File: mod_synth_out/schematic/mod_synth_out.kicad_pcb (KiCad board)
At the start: 2 copper layers, 74.3 x 109.2 mm, 64 parts, among them J1 L IN, J2 R IN, J3 Conn_02x08_Odd_Even, J4 Phones, J5 L OUT, J6 R OUT, Q1 2N3904, Q2 2N3904, U1 TL072, U2 TL072, U3 NE5532, U4 NE5532

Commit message: Attmept layout of output pcb on large pcb
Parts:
- added J7: Conn_01x07_Female, Connector_PinSocket_2.54mm:PinSocket_1x07_P2.54mm_Vertical, F.Cu at (207.6, 79.4)
- added J8: Conn_01x07_Male, Connector_PinHeader_2.54mm:PinHeader_1x07_P2.54mm_Vertical, B.Cu at (250.2, 79.4)
- C1, C10, C11, C12, C13, C14, C15, C16, C2, C3, C4, C5, C6, C7, C8, C9, D1, D2, D3, D4, D7, D8, FB1, FB2, J3, Q1, Q2, R1, R10, R11, R12, R13, R14, R15, R16, R17, R18, R19, R2, R20, R21, R22, R23, R24, R3, R4, R5, R6, R7, R8, R9, U1, U2, U3, U4: moved to B.Cu
- moved D1 218.8 mm to (233.0, 45.7), turned to 270 degrees
- moved R2 217.4 mm to (275.6, 83.2)
- moved D2 214.0 mm to (233.0, 35.6), turned to 270 degrees
- moved R18 194.0 mm to (217.8, 35.6), turned to 0 degrees
- moved J2 193.1 mm to (258.4, 61.6)
- moved RV2 191.8 mm to (265.4, 116.2)
- moved R1 190.1 mm to (248.9, 83.2)
- moved R17 185.2 mm to (210.2, 35.6), turned to 180 degrees
- moved D4 180.9 mm to (196.2, 35.6)
- moved D3 176.6 mm to (196.2, 53.3), turned to 90 degrees
- moved J1 175.4 mm to (242.6, 61.6)
- moved RV1 172.9 mm to (243.2, 116.2)
- moved J4 170.2 mm to (224.2, 132.7)
- moved J6 169.6 mm to (222.9, 45.7)
- moved R20 163.2 mm to (229.2, 55.9), turned to 180 degrees
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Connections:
- C10 pad 1: GND -> /GND_PCB_B
- C10 pad 2: +12V -> /+12_PCB_B
- C7 pad 1: -12V -> /-12_PCB_B
- C7 pad 2: GND -> /GND_PCB_B
- D5 pad 2: +12V -> /+12_PCB_B
- D6 pad 2: +12V -> /+12_PCB_B
- J1 pad S: GND -> /GND_PCB_B
- J2 pad S: GND -> /GND_PCB_B
- Q1 pad 1: GND -> /GND_PCB_B
- Q2 pad 1: GND -> /GND_PCB_B
- RV1 pad 1: GND -> /GND_PCB_B
- RV1 pad 4: GND -> /GND_PCB_B
- RV2 pad 1: GND -> /GND_PCB_B
- RV2 pad 4: GND -> /GND_PCB_B
- U1 pad 3: GND -> /GND_PCB_B
- U1 pad 4: -12V -> /-12_PCB_B
- U1 pad 5: GND -> /GND_PCB_B
- U1 pad 8: +12V -> /+12_PCB_B
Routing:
- net +12V: track 0.00 -> 187.8 mm
- net -12V: track 0.00 -> 142.3 mm
- net Net-(C16-Pad1): track 0.00 -> 55.9 mm
- net Net-(C6-Pad2): track 0.00 -> 54.6 mm
- net Net-(C15-Pad1): track 0.00 -> 52.8 mm
- net /A_POT_PH_R: track 0.00 -> 51.6 mm
- net /A_POT_MR: track 0.00 -> 48.7 mm
- net Net-(C9-Pad2): track 0.00 -> 48.5 mm
- net Net-(C5-Pad1): track 0.00 -> 46.1 mm
- net /A_POT_ML: track 0.00 -> 44.3 mm
- net Net-(C8-Pad2): track 0.00 -> 44.1 mm
- net Net-(C6-Pad1): track 0.00 -> 43.7 mm
- net /A_POT_PH_L: track 0.00 -> 41.8 mm
- net Net-(R7-Pad1): track 0.00 -> 41.5 mm
- net Net-(R10-Pad2): track 0.00 -> 41.2 mm
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- added copper zone on B.Cu, net /GND_PCB_B
- added copper zone on F.Cu, net /GND_PCB_B
- added copper zone on B.Cu, net GND
- added copper zone on F.Cu, net GND
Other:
- board size 74.3 x 109.2 mm -> 81.9 x 109.2 mm

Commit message: Finish huge output pcb
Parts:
- moved U3 10.8 mm to (201.3, 98.4), turned to 0 degrees
- moved U4 10.8 mm to (220.3, 98.4), turned to 0 degrees
- moved U1 10.3 mm to (253.4, 97.8), turned to 0 degrees
- moved D1 8.26 mm to (233.0, 54.0), turned to 90 degrees
- moved C8 2.54 mm to (248.3, 95.9), turned to 270 degrees
- moved C9 2.54 mm to (266.1, 95.9), turned to 270 degrees
- moved J7 0.64 mm to (207.0, 79.4)
- moved C7 0.64 mm to (254.6, 86.4)
- moved D2 0.63 mm to (233.0, 36.2)
- moved D3 0.63 mm to (196.2, 54.0)
- moved D4 0.63 mm to (196.2, 36.2)
- moved R17 0.63 mm to (210.2, 36.2)
- moved R18 0.63 mm to (217.8, 36.2)
- moved C5 0.63 mm to (241.9, 87.0)
- moved J8 0.63 mm to (249.6, 79.4)
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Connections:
- J5 pad S: Net-(J5-PadS) -> GND
- J6 pad S: Net-(J6-PadS) -> GND
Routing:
- net Net-(R14-Pad2): track 16.2 -> 48.2 mm
- net Net-(C6-Pad1): track 43.7 -> 15.1 mm
- net -12V: track 142.3 -> 170.7 mm
- net Net-(C6-Pad2): track 54.6 -> 26.7 mm
- net Net-(C5-Pad1): track 46.1 -> 22.5 mm
- net +12V: track 187.8 -> 164.3 mm
- net Net-(R7-Pad1): track 41.5 -> 20.7 mm
- net Net-(R10-Pad2): track 41.2 -> 20.7 mm
- net /GND_PCB_B: track 16.7 -> 0.00 mm
- net /+12_PCB_B: track 39.8 -> 52.5 mm
- net Net-(C5-Pad2): track 26.8 -> 15.6 mm
- net Net-(J4-PadT): track 38.7 -> 49.5 mm
- net Net-(R13-Pad2): track 7.93 -> 15.1 mm
- net Net-(R15-Pad2): track 7.93 -> 14.1 mm
- net /A_POT_ML: track 44.3 -> 39.5 mm
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
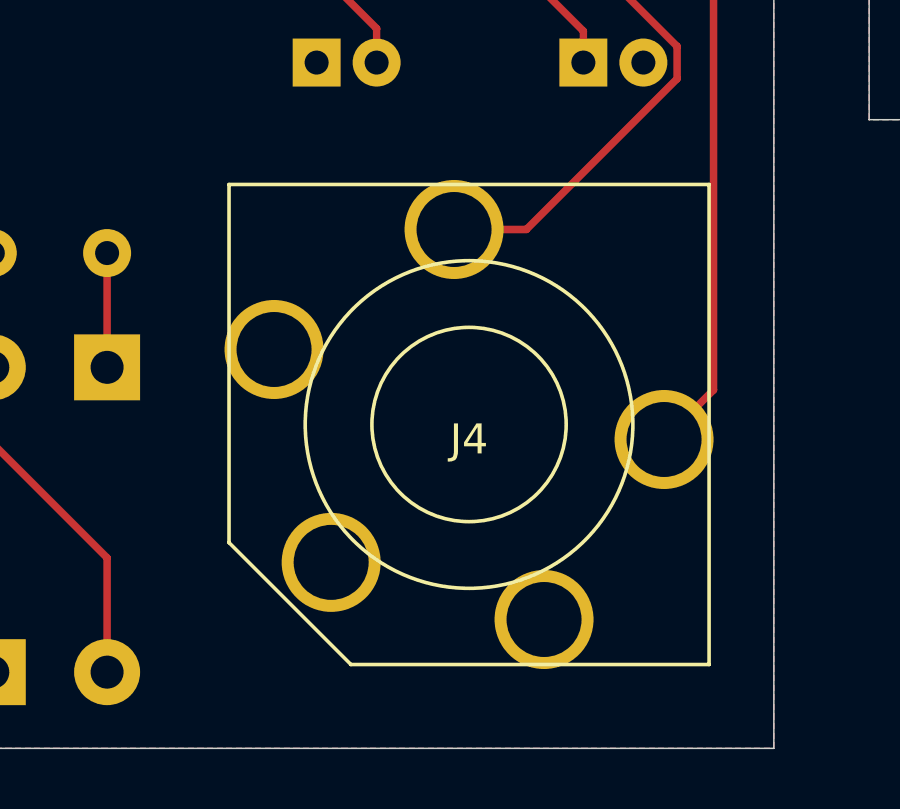
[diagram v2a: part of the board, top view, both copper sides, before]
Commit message: Align headphone output
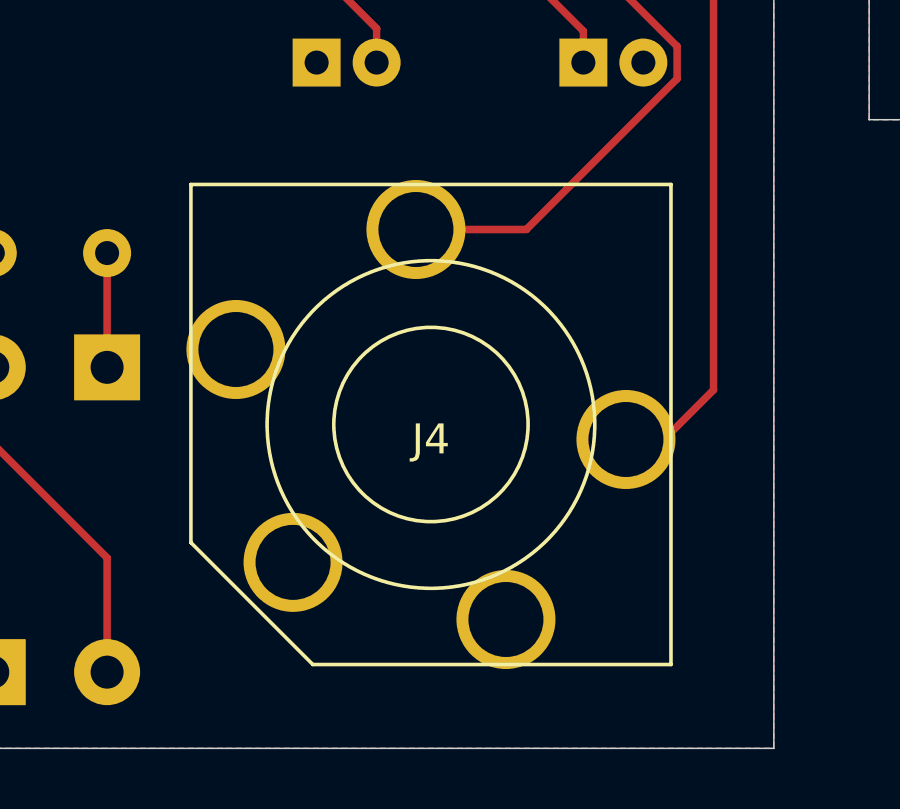
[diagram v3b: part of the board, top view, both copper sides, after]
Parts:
- moved J4 1.27 mm to (222.9, 132.7)
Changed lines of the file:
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@@
   )
   (module mod_synth:WQP-PJ612A-A (layer F.Cu)
-    (at 224.155 132.715)
+    (at 222.885 132.715)
     (fp_text reference J4 (at 0 0.5) (layer F.SilkS)
       (effects (font (size 1 1) (thickness 0.15)))
